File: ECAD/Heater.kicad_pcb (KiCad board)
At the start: 2 copper layers, 200 x 200 mm, 535 parts, among them J1 Conn_01x01_Female, J2 Conn_01x01_Female

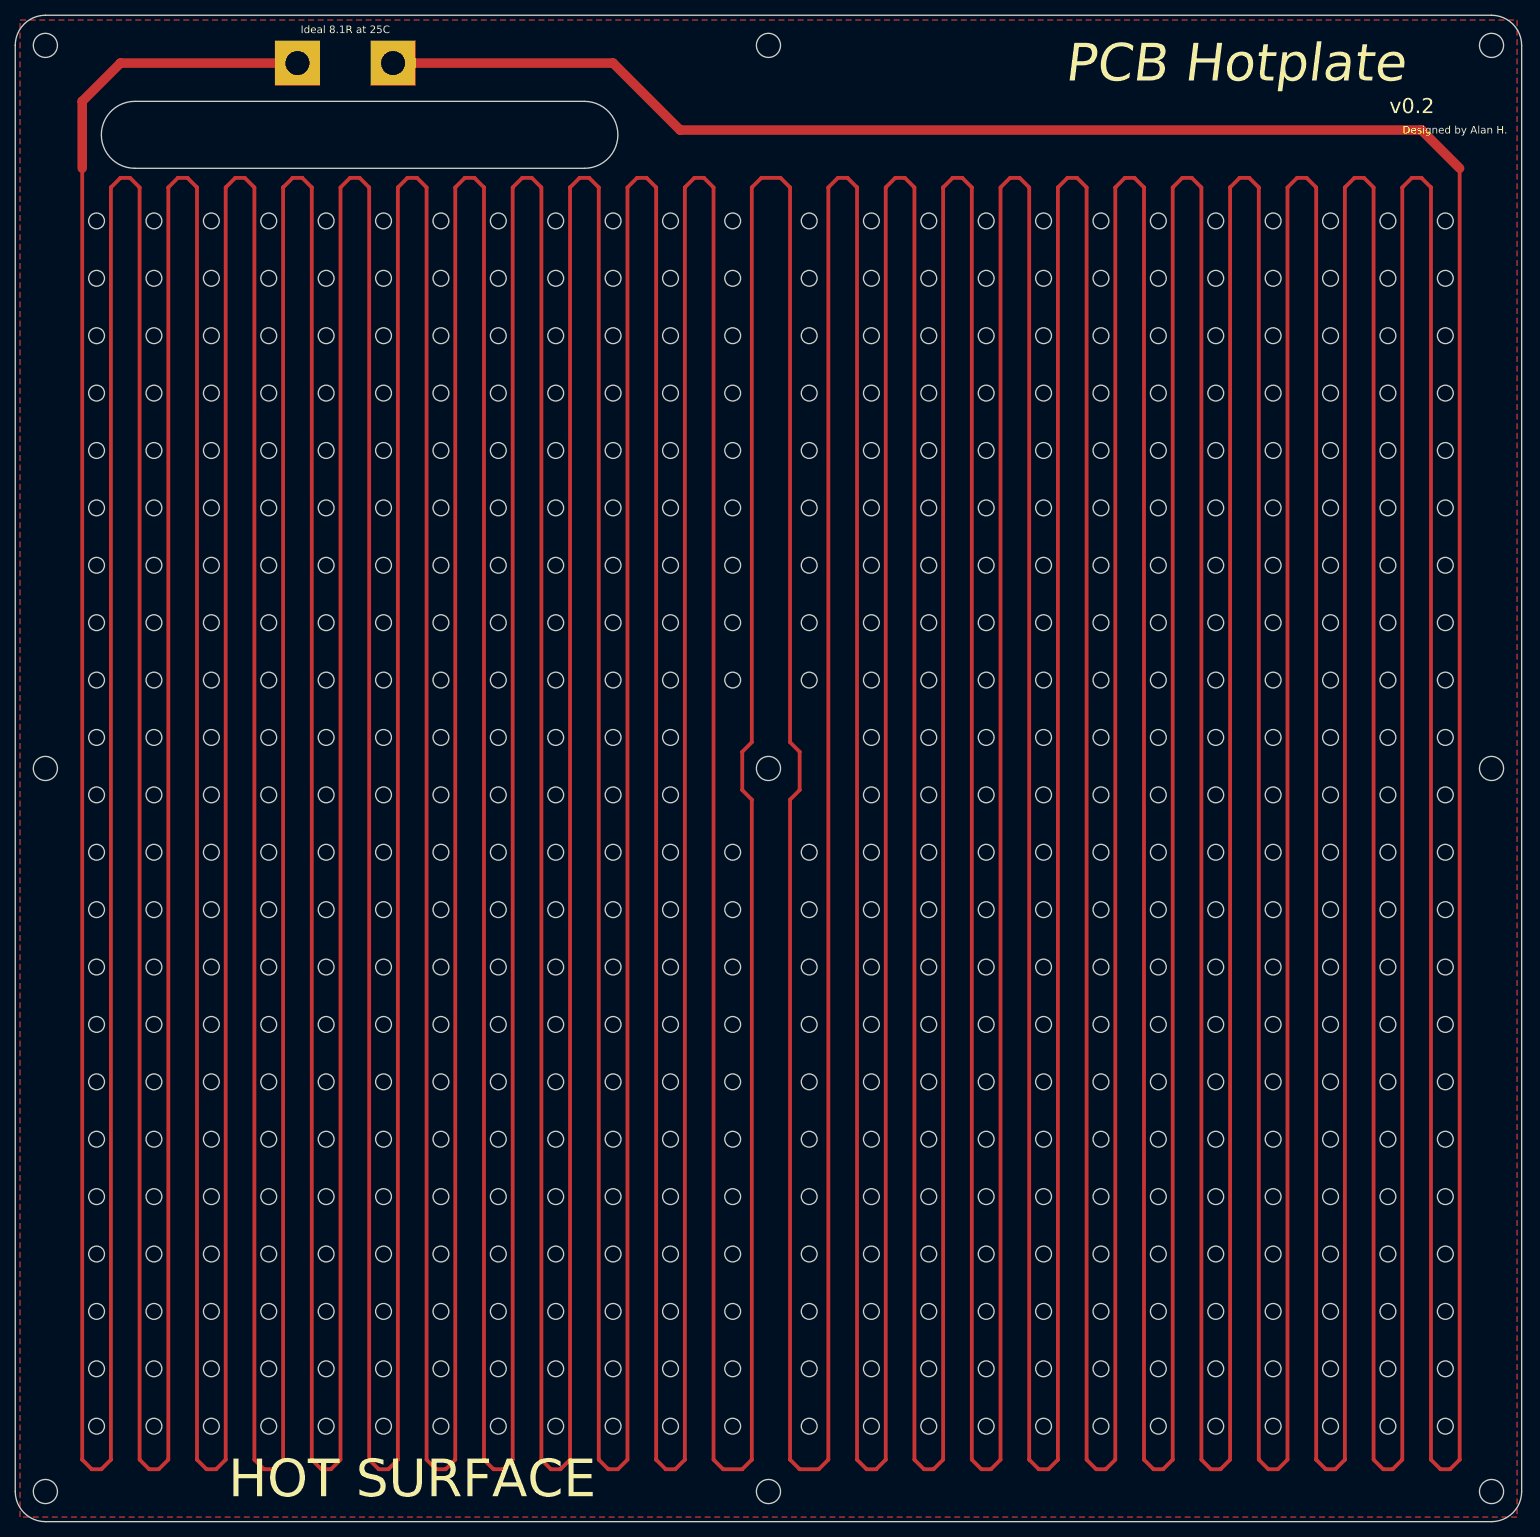
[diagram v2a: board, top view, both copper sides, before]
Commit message: Widened traces to 30mil
In order to reduce resistance and increase wattage, traces widened up to 30mil (theoretical 5.4R at 25C)
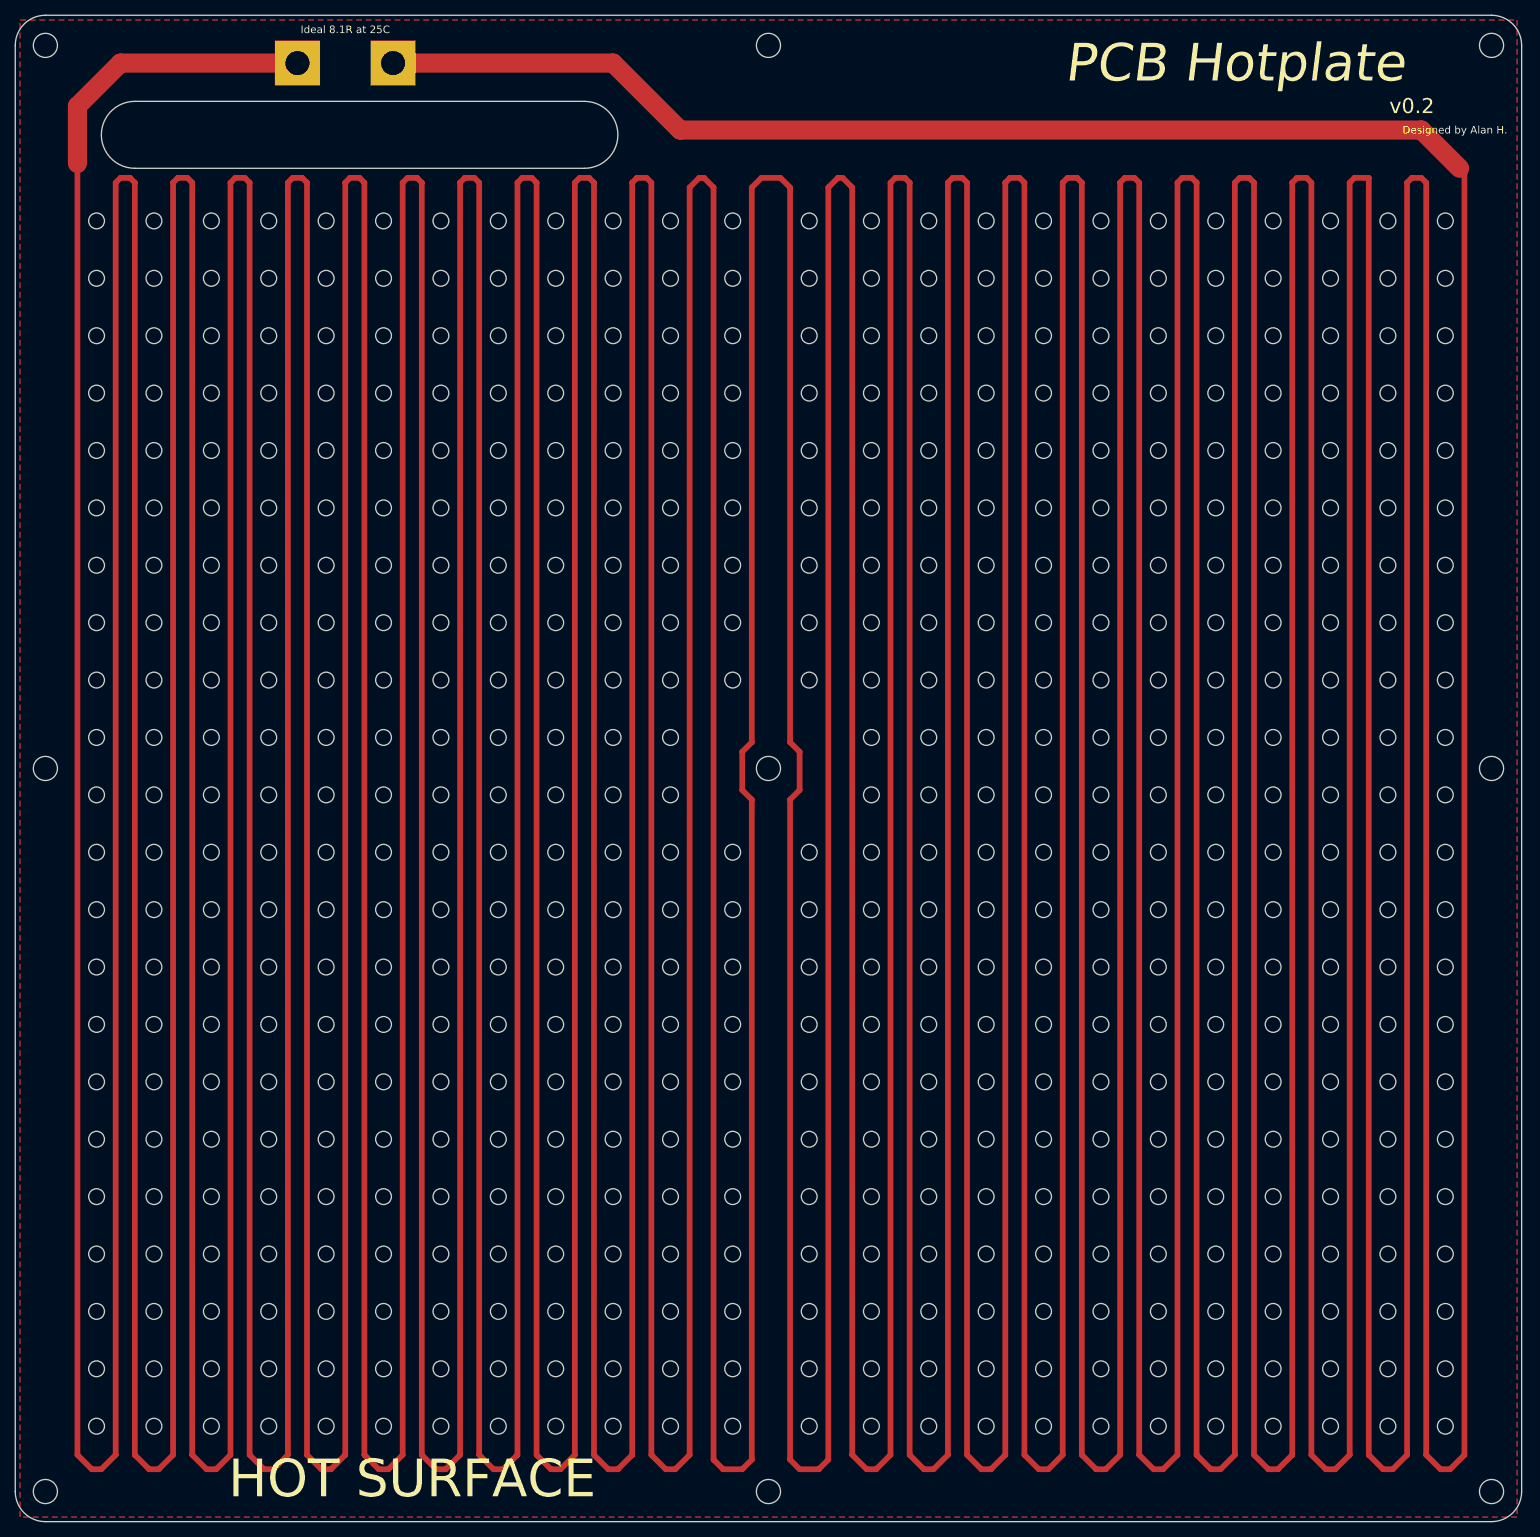
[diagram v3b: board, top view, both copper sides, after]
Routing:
- net Net-(J1-Pad1): track 8534.2 -> 8534.8 mm

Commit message: Revert "Perforated heater"
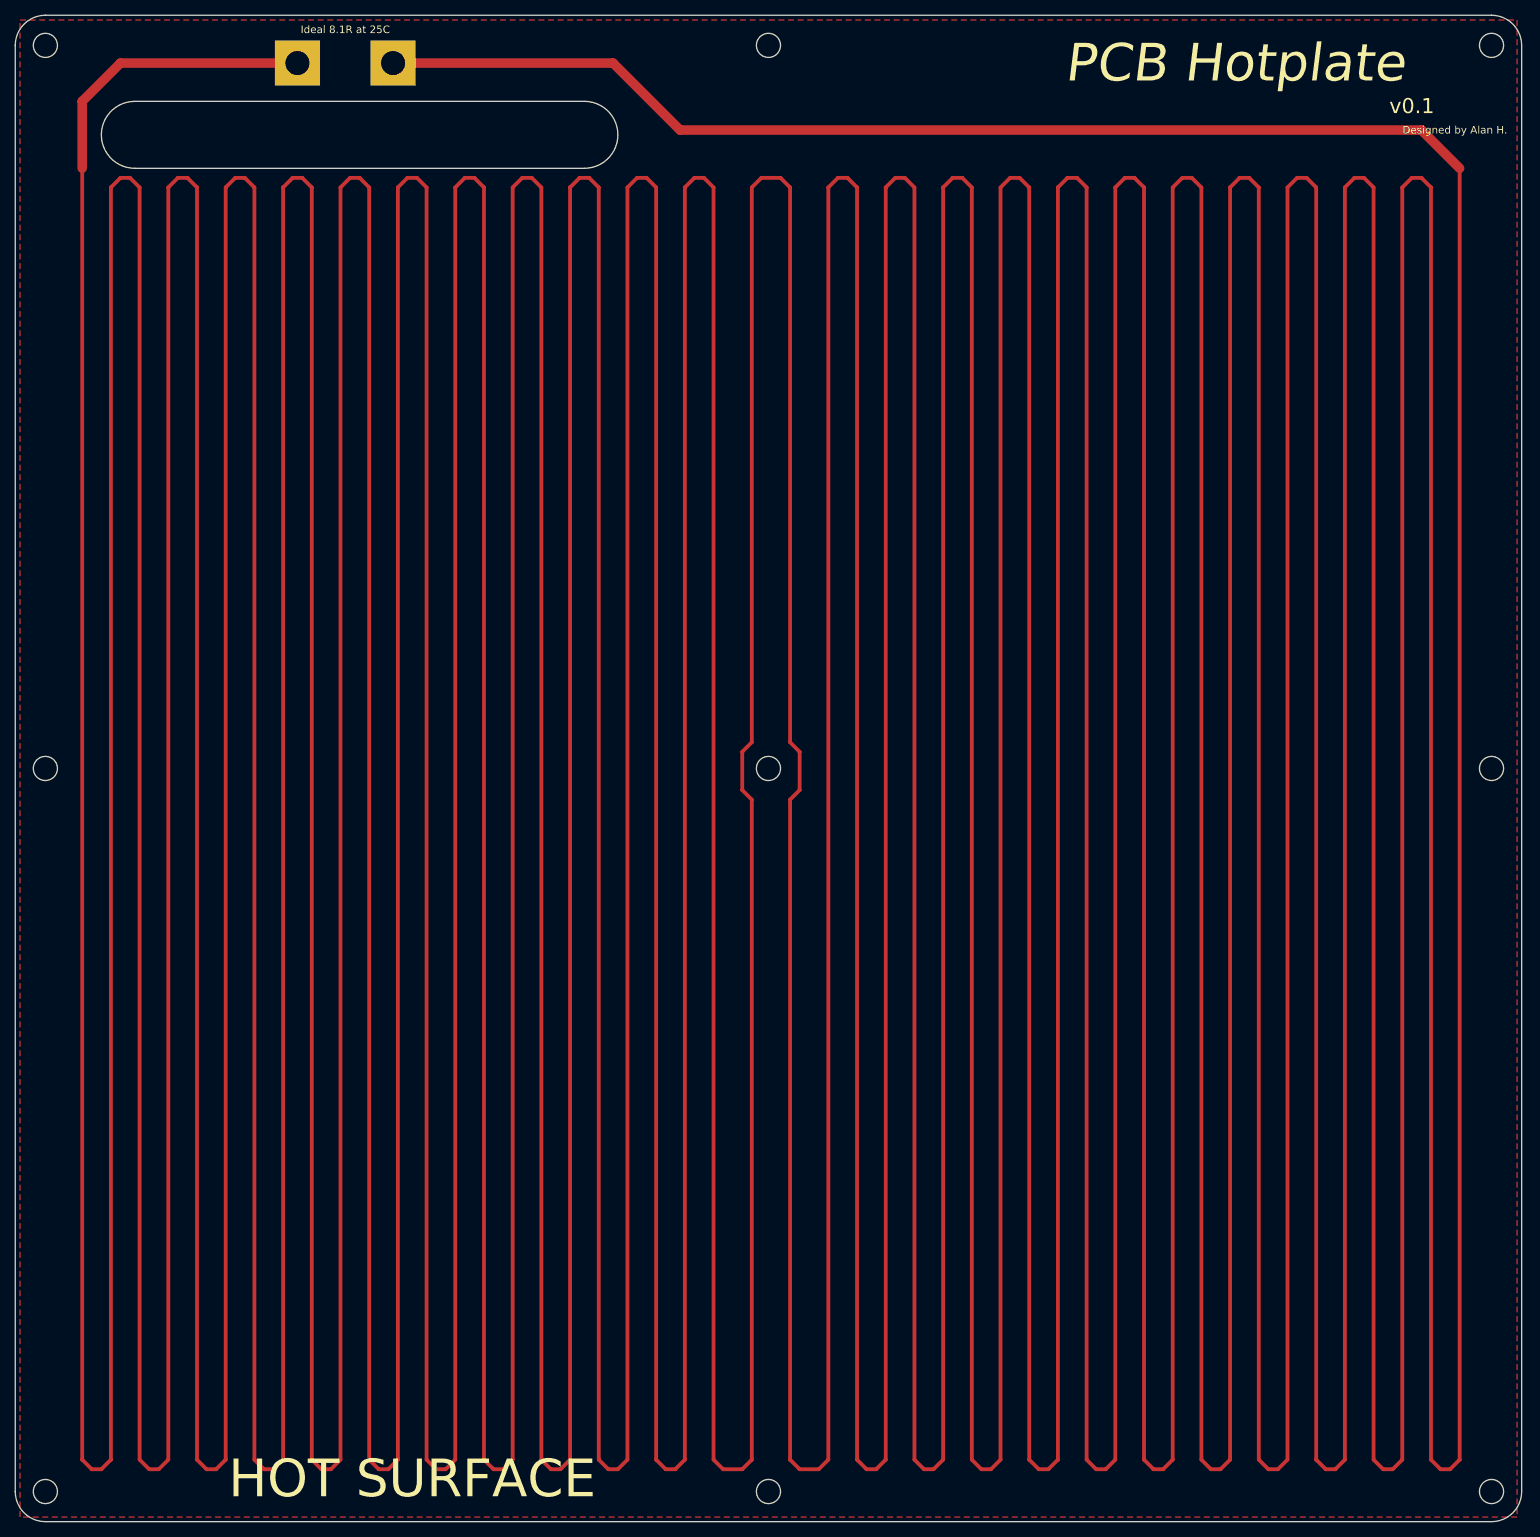
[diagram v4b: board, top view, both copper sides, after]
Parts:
- removed the REF** at (97.2, 37.5)
- removed the REF** at (81.9, 37.5)
- removed the REF** at (146.7, 67.9)
- removed the REF** at (89.5, 67.9)
- removed the REF** at (139.1, 67.9)
- removed the REF** at (123.8, 67.9)
- removed the REF** at (105.4, 67.9)
- removed the REF** at (115.6, 67.9)
- removed the REF** at (81.9, 67.9)
- removed the REF** at (74.3, 67.9)
- removed the REF** at (66.7, 67.9)
- removed the REF** at (51.4, 67.9)
- removed the REF** at (74.3, 37.5)
- removed the REF** at (59.1, 67.9)
- removed the REF** at (43.8, 67.9)
- removed the REF** at (28.6, 67.9)
- removed the REF** at (21.0, 67.9)
- removed the REF** at (200.0, 75.6)
- removed the REF** at (192.4, 75.6)
- removed the REF** at (184.8, 75.6)
- removed the REF** at (177.2, 75.6)
- removed the REF** at (169.5, 75.6)
- removed the REF** at (146.7, 75.6)
- removed the REF** at (66.7, 37.5)
- removed the REF** at (161.9, 75.6)
- removed the REF** at (154.3, 75.6)
- removed the REF** at (139.1, 75.6)
- removed the REF** at (131.4, 75.6)
- removed the REF** at (123.8, 75.6)
- removed the REF** at (115.6, 75.6)
- removed the REF** at (105.4, 75.6)
- removed the REF** at (97.2, 75.6)
- removed the REF** at (89.5, 75.6)
- removed the REF** at (51.4, 75.6)
- removed the REF** at (51.4, 37.5)
- removed the REF** at (43.8, 75.6)
- removed the REF** at (36.2, 75.6)
- removed the REF** at (36.2, 67.9)
- removed the REF** at (66.7, 75.6)
- removed the REF** at (81.9, 75.6)
- removed the REF** at (59.1, 75.6)
- removed the REF** at (74.3, 75.6)
- removed the REF** at (28.6, 75.6)
- removed the REF** at (21.0, 75.6)
- removed the REF** at (192.4, 67.9)
- removed the REF** at (59.1, 37.5)
- removed the REF** at (161.9, 67.9)
- removed the REF** at (169.5, 67.9)
- removed the REF** at (184.8, 67.9)
- removed the REF** at (200.0, 67.9)
- removed the REF** at (177.2, 67.9)
- removed the REF** at (97.2, 83.2)
- removed the REF** at (131.4, 83.2)
- removed the REF** at (154.3, 83.2)
- removed the REF** at (146.7, 83.2)
- removed the REF** at (89.5, 83.2)
- removed the REF** at (43.8, 37.5)
- removed the REF** at (139.1, 83.2)
- removed the REF** at (123.8, 83.2)
- removed the REF** at (105.4, 83.2)
- removed the REF** at (115.6, 83.2)
- removed the REF** at (81.9, 83.2)
- removed the REF** at (74.3, 83.2)
- removed the REF** at (66.7, 83.2)
- removed the REF** at (51.4, 83.2)
- removed the REF** at (59.1, 83.2)
- removed the REF** at (43.8, 83.2)
- removed the REF** at (28.6, 37.5)
- removed the REF** at (28.6, 83.2)
- removed the REF** at (21.0, 83.2)
- removed the REF** at (200.0, 90.8)
- removed the REF** at (192.4, 90.8)
- removed the REF** at (184.8, 90.8)
- removed the REF** at (177.2, 90.8)
- removed the REF** at (169.5, 90.8)
- removed the REF** at (146.7, 90.8)
- removed the REF** at (161.9, 90.8)
- removed the REF** at (154.3, 90.8)
- removed the REF** at (21.0, 37.5)
- removed the REF** at (139.1, 90.8)
- removed the REF** at (131.4, 90.8)
- removed the REF** at (123.8, 90.8)
- removed the REF** at (115.6, 90.8)
- removed the REF** at (105.4, 90.8)
- removed the REF** at (97.2, 90.8)
- removed the REF** at (89.5, 90.8)
- removed the REF** at (51.4, 90.8)
- removed the REF** at (43.8, 90.8)
- removed the REF** at (36.2, 90.8)
- removed the REF** at (200.0, 45.1)
- removed the REF** at (36.2, 83.2)
- removed the REF** at (66.7, 90.8)
- removed the REF** at (81.9, 90.8)
- removed the REF** at (59.1, 90.8)
- removed the REF** at (74.3, 90.8)
- removed the REF** at (28.6, 90.8)
- removed the REF** at (21.0, 90.8)
- removed the REF** at (192.4, 83.2)
- removed the REF** at (161.9, 83.2)
- removed the REF** at (169.5, 83.2)
- removed the REF** at (192.4, 45.1)
- removed the REF** at (184.8, 83.2)
- removed the REF** at (200.0, 83.2)
- removed the REF** at (177.2, 83.2)
- removed the REF** at (97.2, 98.4)
- removed the REF** at (131.4, 98.4)
- removed the REF** at (154.3, 98.4)
- removed the REF** at (146.7, 98.4)
- removed the REF** at (89.5, 98.4)
- removed the REF** at (139.1, 98.4)
- removed the REF** at (123.8, 98.4)
- removed the REF** at (131.4, 37.5)
- removed the REF** at (184.8, 45.1)
- removed the REF** at (105.4, 98.4)
- removed the REF** at (115.6, 98.4)
- removed the REF** at (81.9, 98.4)
- removed the REF** at (74.3, 98.4)
- removed the REF** at (66.7, 98.4)
- removed the REF** at (51.4, 98.4)
- removed the REF** at (59.1, 98.4)
- removed the REF** at (43.8, 98.4)
- removed the REF** at (28.6, 98.4)
- removed the REF** at (21.0, 98.4)
- removed the REF** at (177.2, 45.1)
- removed the REF** at (200.0, 106.0)
- removed the REF** at (192.4, 106.0)
- removed the REF** at (184.8, 106.0)
- removed the REF** at (177.2, 106.0)
- removed the REF** at (169.5, 106.0)
- removed the REF** at (146.7, 106.0)
- removed the REF** at (161.9, 106.0)
- removed the REF** at (154.3, 106.0)
- removed the REF** at (139.1, 106.0)
- removed the REF** at (131.4, 106.0)
- removed the REF** at (169.5, 45.1)
- removed the REF** at (123.8, 106.0)
- removed the REF** at (97.2, 106.0)
- removed the REF** at (89.5, 106.0)
- removed the REF** at (51.4, 106.0)
- removed the REF** at (43.8, 106.0)
- removed the REF** at (36.2, 106.0)
- removed the REF** at (36.2, 98.4)
- removed the REF** at (66.7, 106.0)
- removed the REF** at (81.9, 106.0)
- removed the REF** at (59.1, 106.0)
- removed the REF** at (146.7, 45.1)
- removed the REF** at (74.3, 106.0)
- removed the REF** at (28.6, 106.0)
- removed the REF** at (21.0, 106.0)
- removed the REF** at (192.4, 98.4)
- removed the REF** at (161.9, 98.4)
- removed the REF** at (169.5, 98.4)
- removed the REF** at (184.8, 98.4)
- removed the REF** at (200.0, 98.4)
- removed the REF** at (177.2, 98.4)
- removed the REF** at (97.2, 113.7)
- removed the REF** at (161.9, 45.1)
- removed the REF** at (131.4, 113.7)
- removed the REF** at (154.3, 113.7)
- removed the REF** at (146.7, 113.7)
- removed the REF** at (89.5, 113.7)
- removed the REF** at (139.1, 113.7)
- removed the REF** at (123.8, 113.7)
- removed the REF** at (81.9, 113.7)
- removed the REF** at (74.3, 113.7)
- removed the REF** at (66.7, 113.7)
- removed the REF** at (51.4, 113.7)
- removed the REF** at (154.3, 45.1)
- removed the REF** at (59.1, 113.7)
- removed the REF** at (43.8, 113.7)
- removed the REF** at (28.6, 113.7)
- removed the REF** at (21.0, 113.7)
- removed the REF** at (200.0, 121.3)
- removed the REF** at (192.4, 121.3)
- removed the REF** at (184.8, 121.3)
- removed the REF** at (177.2, 121.3)
- removed the REF** at (169.5, 121.3)
- removed the REF** at (146.7, 121.3)
- removed the REF** at (139.1, 45.1)
- removed the REF** at (161.9, 121.3)
- removed the REF** at (154.3, 121.3)
- removed the REF** at (139.1, 121.3)
- removed the REF** at (131.4, 121.3)
- removed the REF** at (123.8, 121.3)
- removed the REF** at (115.6, 121.3)
- removed the REF** at (105.4, 121.3)
- removed the REF** at (97.2, 121.3)
- removed the REF** at (89.5, 121.3)
- removed the REF** at (51.4, 121.3)
- removed the REF** at (131.4, 45.1)
- removed the REF** at (43.8, 121.3)
- removed the REF** at (36.2, 121.3)
- removed the REF** at (36.2, 113.7)
- removed the REF** at (66.7, 121.3)
- removed the REF** at (81.9, 121.3)
- removed the REF** at (59.1, 121.3)
- removed the REF** at (74.3, 121.3)
- removed the REF** at (28.6, 121.3)
- removed the REF** at (21.0, 121.3)
- removed the REF** at (192.4, 113.7)
- removed the REF** at (123.8, 45.1)
- removed the REF** at (161.9, 113.7)
- removed the REF** at (169.5, 113.7)
- removed the REF** at (184.8, 113.7)
- removed the REF** at (200.0, 113.7)
- removed the REF** at (177.2, 113.7)
- removed the REF** at (97.2, 128.9)
- removed the REF** at (131.4, 128.9)
- removed the REF** at (154.3, 128.9)
- removed the REF** at (146.7, 128.9)
- removed the REF** at (89.5, 128.9)
- removed the REF** at (115.6, 45.1)
- removed the REF** at (139.1, 128.9)
- removed the REF** at (123.8, 128.9)
- removed the REF** at (105.4, 128.9)
- removed the REF** at (115.6, 128.9)
- removed the REF** at (81.9, 128.9)
- removed the REF** at (74.3, 128.9)
- removed the REF** at (66.7, 128.9)
- removed the REF** at (51.4, 128.9)
- removed the REF** at (59.1, 128.9)
- removed the REF** at (43.8, 128.9)
- removed the REF** at (154.3, 37.5)
- removed the REF** at (105.4, 45.1)
- removed the REF** at (28.6, 128.9)
- removed the REF** at (21.0, 128.9)
- removed the REF** at (200.0, 136.5)
- removed the REF** at (192.4, 136.5)
- removed the REF** at (184.8, 136.5)
- removed the REF** at (177.2, 136.5)
- removed the REF** at (169.5, 136.5)
- removed the REF** at (146.7, 136.5)
- removed the REF** at (161.9, 136.5)
- removed the REF** at (154.3, 136.5)
- removed the REF** at (97.2, 45.1)
- removed the REF** at (139.1, 136.5)
- removed the REF** at (131.4, 136.5)
- removed the REF** at (123.8, 136.5)
- removed the REF** at (115.6, 136.5)
- removed the REF** at (105.4, 136.5)
- removed the REF** at (97.2, 136.5)
- removed the REF** at (89.5, 136.5)
- removed the REF** at (51.4, 136.5)
- removed the REF** at (43.8, 136.5)
- removed the REF** at (36.2, 136.5)
- removed the REF** at (89.5, 45.1)
- removed the REF** at (36.2, 128.9)
- removed the REF** at (66.7, 136.5)
- removed the REF** at (81.9, 136.5)
- removed the REF** at (59.1, 136.5)
- removed the REF** at (74.3, 136.5)
- removed the REF** at (28.6, 136.5)
- removed the REF** at (21.0, 136.5)
- removed the REF** at (192.4, 128.9)
- removed the REF** at (161.9, 128.9)
- removed the REF** at (169.5, 128.9)
- removed the REF** at (51.4, 45.1)
- removed the REF** at (184.8, 128.9)
- removed the REF** at (200.0, 128.9)
- removed the REF** at (177.2, 128.9)
- removed the REF** at (97.2, 144.1)
- removed the REF** at (131.4, 144.1)
- removed the REF** at (154.3, 144.1)
- removed the REF** at (146.7, 144.1)
- removed the REF** at (89.5, 144.1)
- removed the REF** at (139.1, 144.1)
- removed the REF** at (123.8, 144.1)
- removed the REF** at (43.8, 45.1)
- removed the REF** at (105.4, 144.1)
- removed the REF** at (115.6, 144.1)
- removed the REF** at (81.9, 144.1)
- removed the REF** at (74.3, 144.1)
- removed the REF** at (66.7, 144.1)
- removed the REF** at (51.4, 144.1)
- removed the REF** at (59.1, 144.1)
- removed the REF** at (43.8, 144.1)
- removed the REF** at (28.6, 144.1)
- removed the REF** at (21.0, 144.1)
- removed the REF** at (36.2, 45.1)
- removed the REF** at (200.0, 151.8)
- removed the REF** at (192.4, 151.8)
- removed the REF** at (184.8, 151.8)
- removed the REF** at (177.2, 151.8)
- removed the REF** at (169.5, 151.8)
- removed the REF** at (146.7, 151.8)
- removed the REF** at (161.9, 151.8)
- removed the REF** at (154.3, 151.8)
- removed the REF** at (139.1, 151.8)
- removed the REF** at (131.4, 151.8)
- removed the REF** at (36.2, 37.5)
- removed the REF** at (123.8, 151.8)
- removed the REF** at (115.6, 151.8)
- removed the REF** at (105.4, 151.8)
- removed the REF** at (97.2, 151.8)
- removed the REF** at (89.5, 151.8)
- removed the REF** at (51.4, 151.8)
- removed the REF** at (43.8, 151.8)
- removed the REF** at (36.2, 151.8)
- removed the REF** at (36.2, 144.1)
- removed the REF** at (66.7, 151.8)
- removed the REF** at (66.7, 45.1)
- removed the REF** at (81.9, 151.8)
- removed the REF** at (59.1, 151.8)
- removed the REF** at (74.3, 151.8)
- removed the REF** at (28.6, 151.8)
- removed the REF** at (21.0, 151.8)
- removed the REF** at (192.4, 144.1)
- removed the REF** at (161.9, 144.1)
- removed the REF** at (169.5, 144.1)
- removed the REF** at (184.8, 144.1)
- removed the REF** at (200.0, 144.1)
- removed the REF** at (81.9, 45.1)
- removed the REF** at (177.2, 144.1)
- removed the REF** at (97.2, 159.4)
- removed the REF** at (131.4, 159.4)
- removed the REF** at (154.3, 159.4)
- removed the REF** at (146.7, 159.4)
- removed the REF** at (89.5, 159.4)
- removed the REF** at (139.1, 159.4)
- removed the REF** at (123.8, 159.4)
- removed the REF** at (105.4, 159.4)
- removed the REF** at (115.6, 159.4)
- removed the REF** at (59.1, 45.1)
- removed the REF** at (81.9, 159.4)
- removed the REF** at (74.3, 159.4)
- removed the REF** at (66.7, 159.4)
- removed the REF** at (51.4, 159.4)
- removed the REF** at (59.1, 159.4)
- removed the REF** at (43.8, 159.4)
- removed the REF** at (28.6, 159.4)
- removed the REF** at (21.0, 159.4)
- removed the REF** at (200.0, 167.0)
- removed the REF** at (192.4, 167.0)
- removed the REF** at (146.7, 37.5)
- removed the REF** at (74.3, 45.1)
- removed the REF** at (184.8, 167.0)
- removed the REF** at (177.2, 167.0)
- removed the REF** at (169.5, 167.0)
- removed the REF** at (146.7, 167.0)
- removed the REF** at (161.9, 167.0)
- removed the REF** at (154.3, 167.0)
- removed the REF** at (139.1, 167.0)
- removed the REF** at (131.4, 167.0)
- removed the REF** at (123.8, 167.0)
- removed the REF** at (115.6, 167.0)
- removed the REF** at (28.6, 45.1)
- removed the REF** at (105.4, 167.0)
- removed the REF** at (97.2, 167.0)
- removed the REF** at (89.5, 167.0)
- removed the REF** at (51.4, 167.0)
- removed the REF** at (43.8, 167.0)
- removed the REF** at (36.2, 167.0)
- removed the REF** at (36.2, 159.4)
- removed the REF** at (66.7, 167.0)
- removed the REF** at (81.9, 167.0)
- removed the REF** at (59.1, 167.0)
- removed the REF** at (21.0, 45.1)
- removed the REF** at (74.3, 167.0)
- removed the REF** at (28.6, 167.0)
- removed the REF** at (21.0, 167.0)
- removed the REF** at (192.4, 159.4)
- removed the REF** at (161.9, 159.4)
- removed the REF** at (169.5, 159.4)
- removed the REF** at (184.8, 159.4)
- removed the REF** at (200.0, 159.4)
- removed the REF** at (177.2, 159.4)
- removed the REF** at (97.2, 174.6)
- removed the REF** at (192.4, 37.5)
- removed the REF** at (131.4, 174.6)
- removed the REF** at (154.3, 174.6)
- removed the REF** at (146.7, 174.6)
- removed the REF** at (89.5, 174.6)
- removed the REF** at (139.1, 174.6)
- removed the REF** at (123.8, 174.6)
- removed the REF** at (105.4, 174.6)
- removed the REF** at (115.6, 174.6)
- removed the REF** at (81.9, 174.6)
- removed the REF** at (74.3, 174.6)
- removed the REF** at (161.9, 37.5)
- removed the REF** at (66.7, 174.6)
- removed the REF** at (51.4, 174.6)
- removed the REF** at (59.1, 174.6)
- removed the REF** at (43.8, 174.6)
- removed the REF** at (28.6, 174.6)
- removed the REF** at (21.0, 174.6)
- removed the REF** at (200.0, 182.2)
- removed the REF** at (192.4, 182.2)
- removed the REF** at (184.8, 182.2)
- removed the REF** at (177.2, 182.2)
- removed the REF** at (169.5, 37.5)
- removed the REF** at (169.5, 182.2)
- removed the REF** at (146.7, 182.2)
- removed the REF** at (161.9, 182.2)
- removed the REF** at (154.3, 182.2)
- removed the REF** at (139.1, 182.2)
- removed the REF** at (131.4, 182.2)
- removed the REF** at (123.8, 182.2)
- removed the REF** at (115.6, 182.2)
- removed the REF** at (105.4, 182.2)
- removed the REF** at (97.2, 182.2)
- removed the REF** at (184.8, 37.5)
- removed the REF** at (89.5, 182.2)
- removed the REF** at (51.4, 182.2)
- removed the REF** at (43.8, 182.2)
- removed the REF** at (36.2, 182.2)
- removed the REF** at (36.2, 174.6)
- removed the REF** at (66.7, 182.2)
- removed the REF** at (81.9, 182.2)
- removed the REF** at (59.1, 182.2)
- removed the REF** at (74.3, 182.2)
- removed the REF** at (28.6, 182.2)
- removed the REF** at (200.0, 37.5)
- removed the REF** at (21.0, 182.2)
- removed the REF** at (192.4, 174.6)
- removed the REF** at (161.9, 174.6)
- removed the REF** at (169.5, 174.6)
- removed the REF** at (184.8, 174.6)
- removed the REF** at (200.0, 174.6)
- removed the REF** at (177.2, 174.6)
- removed the REF** at (200.0, 189.9)
- removed the REF** at (192.4, 189.9)
- removed the REF** at (184.8, 189.9)
- removed the REF** at (177.2, 37.5)
- removed the REF** at (177.2, 189.9)
- removed the REF** at (169.5, 189.9)
- removed the REF** at (161.9, 189.9)
- removed the REF** at (154.3, 189.9)
- removed the REF** at (146.7, 189.9)
- removed the REF** at (139.1, 189.9)
- removed the REF** at (131.4, 189.9)
- removed the REF** at (123.8, 189.9)
- removed the REF** at (115.6, 189.9)
- removed the REF** at (105.4, 189.9)
- removed the REF** at (97.2, 52.7)
- removed the REF** at (97.2, 189.9)
- removed the REF** at (89.5, 189.9)
- removed the REF** at (81.9, 189.9)
- removed the REF** at (74.3, 189.9)
- removed the REF** at (66.7, 189.9)
- removed the REF** at (59.1, 189.9)
- removed the REF** at (51.4, 189.9)
- removed the REF** at (43.8, 189.9)
- removed the REF** at (36.2, 189.9)
- removed the REF** at (28.6, 189.9)
- removed the REF** at (89.5, 37.5)
- removed the REF** at (131.4, 52.7)
- removed the REF** at (21.0, 189.9)
- removed the REF** at (200.0, 197.5)
- removed the REF** at (192.4, 197.5)
- removed the REF** at (184.8, 197.5)
- removed the REF** at (177.2, 197.5)
- removed the REF** at (169.5, 197.5)
- removed the REF** at (161.9, 197.5)
- removed the REF** at (154.3, 197.5)
- removed the REF** at (146.7, 197.5)
- removed the REF** at (139.1, 197.5)
- removed the REF** at (154.3, 52.7)
- removed the REF** at (131.4, 197.5)
- removed the REF** at (123.8, 197.5)
- removed the REF** at (115.6, 197.5)
- removed the REF** at (105.4, 197.5)
- removed the REF** at (97.2, 197.5)
- removed the REF** at (89.5, 197.5)
- removed the REF** at (81.9, 197.5)
- removed the REF** at (74.3, 197.5)
- removed the REF** at (66.7, 197.5)
- removed the REF** at (59.1, 197.5)
- removed the REF** at (146.7, 52.7)
- removed the REF** at (51.4, 197.5)
- removed the REF** at (43.8, 197.5)
- removed the REF** at (36.2, 197.5)
- removed the REF** at (28.6, 197.5)
- removed the REF** at (21.0, 197.5)
- removed the REF** at (89.5, 52.7)
- removed the REF** at (139.1, 52.7)
- removed the REF** at (123.8, 52.7)
- removed the REF** at (105.4, 52.7)
- removed the REF** at (115.6, 52.7)
- removed the REF** at (81.9, 52.7)
- removed the REF** at (74.3, 52.7)
- removed the REF** at (139.1, 37.5)
- removed the REF** at (66.7, 52.7)
- removed the REF** at (51.4, 52.7)
- removed the REF** at (59.1, 52.7)
- removed the REF** at (43.8, 52.7)
- removed the REF** at (28.6, 52.7)
- removed the REF** at (21.0, 52.7)
- removed the REF** at (200.0, 60.3)
- removed the REF** at (192.4, 60.3)
- removed the REF** at (184.8, 60.3)
- removed the REF** at (177.2, 60.3)
- removed the REF** at (123.8, 37.5)
- removed the REF** at (169.5, 60.3)
- removed the REF** at (146.7, 60.3)
- removed the REF** at (161.9, 60.3)
- removed the REF** at (154.3, 60.3)
- removed the REF** at (139.1, 60.3)
- removed the REF** at (131.4, 60.3)
- removed the REF** at (123.8, 60.3)
- removed the REF** at (115.6, 60.3)
- removed the REF** at (105.4, 60.3)
- removed the REF** at (97.2, 60.3)
- removed the REF** at (105.4, 37.5)
- removed the REF** at (89.5, 60.3)
- removed the REF** at (51.4, 60.3)
- removed the REF** at (43.8, 60.3)
- removed the REF** at (36.2, 60.3)
- removed the REF** at (36.2, 52.7)
- removed the REF** at (66.7, 60.3)
- removed the REF** at (81.9, 60.3)
- removed the REF** at (59.1, 60.3)
- removed the REF** at (74.3, 60.3)
- removed the REF** at (28.6, 60.3)
- removed the REF** at (115.6, 37.5)
- removed the REF** at (21.0, 60.3)
- removed the REF** at (192.4, 52.7)
- removed the REF** at (161.9, 52.7)
- removed the REF** at (169.5, 52.7)
- removed the REF** at (184.8, 52.7)
- removed the REF** at (200.0, 52.7)
- removed the REF** at (177.2, 52.7)
- removed the REF** at (97.2, 67.9)
- removed the REF** at (131.4, 67.9)
- removed the REF** at (154.3, 67.9)
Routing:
- net Net-(J1-Pad1): track 8534.8 -> 8534.2 mm
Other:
- board text added: "v0.1"
- board text removed: "v0.2"
